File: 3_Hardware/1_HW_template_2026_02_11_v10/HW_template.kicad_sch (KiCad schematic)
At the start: 5 parts, among them P1 ${SIM.PARAMS}, P2 ${SIM.PARAMS}

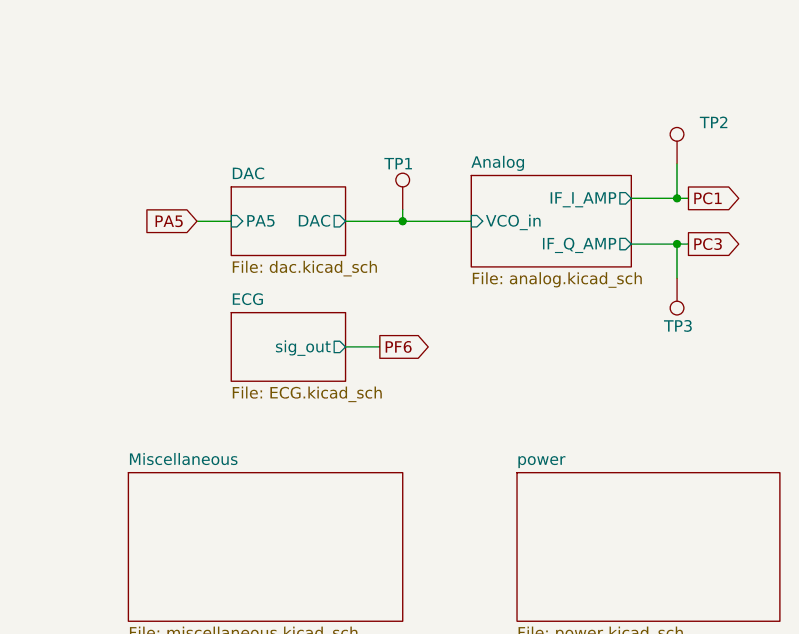
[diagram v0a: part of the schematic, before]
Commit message: pcb - minor naming improvements
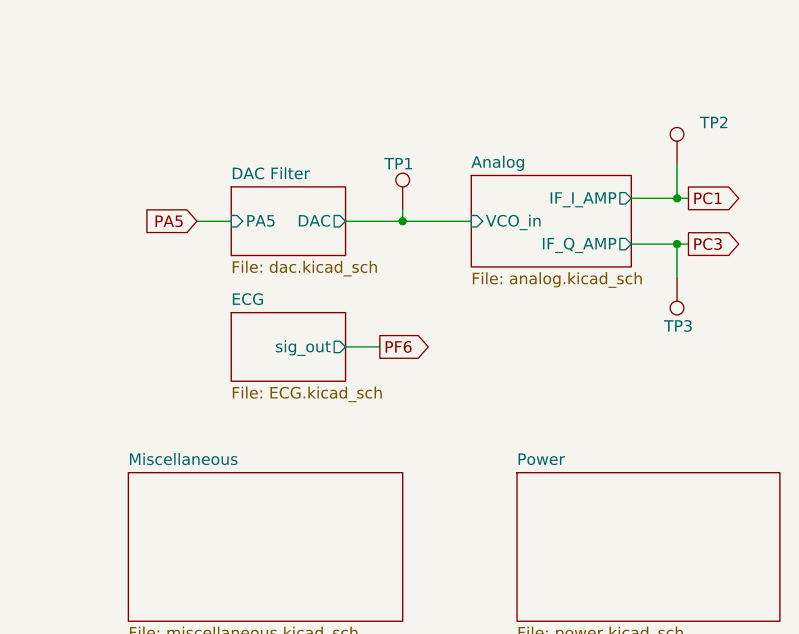
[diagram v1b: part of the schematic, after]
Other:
- sheet DAC renamed DAC Filter
- sheet power renamed Power
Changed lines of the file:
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@@
 			(color 0 0 0 0.0000)
 		)
-		(property "Sheetname" "power"
+		(property "Sheetname" "Power"
 			(at 187.96 99.6184 0)
 			(effects
@@
 			(color 0 0 0 0.0000)
 		)
-		(property "Sheetname" "DAC"
+		(property "Sheetname" "DAC Filter"
 			(at 156.21 67.8684 0)
 			(effects

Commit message: minor pcb improvements + bom
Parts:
- P1, P2: value ${SIM.PARAMS} -> Conn_01x32_Female
- TP1, TP2: value Channel1 -> ~
- TP3: value ${SIM.PARAMS} -> ~
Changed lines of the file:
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@@
 			)
 		)
-		(property "Value" "Channel1"
+		(property "Value" "~"
 			(at 177.8 69.0879 0)
 			(effects
@@
 			)
 		)
-		(property "Value" "${SIM.PARAMS}"
+		(property "Value" "Conn_01x32_Female"
 			(at 62.23 86.3601 0)
 			(effects
@@
 			)
 		)
-		(property "Value" "${SIM.PARAMS}"
+		(property "Value" "~"
 			(at 203.2 80.7721 0)
 			(effects
@@
 			)
 		)
-		(property "Value" "${SIM.PARAMS}"
+		(property "Value" "Conn_01x32_Female"
 			(at 24.13 86.3601 0)
 			(effects
@@
 			)
 		)
-		(property "Value" "Channel1"
+		(property "Value" "~"
 			(at 208.28 64.0079 0)
 			(effects

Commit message: pcb minor improvements
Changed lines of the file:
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@@
+	(wire
+		(pts
+			(xy 31.75 48.26) (xy 30.48 48.26)
+		)
+		(stroke
+			(width 0)
+			(type default)
+		)
+	)
 	(wire
 		(pts
@@
 	(symbol
 		(lib_id "power:GND")
-		(at 30.48 48.26 90)
+		(at 31.75 48.26 90)
 		(mirror x)
 		(unit 1)
@@
 		(fields_autoplaced yes)
 		(property "Reference" "#PWR01"
+			(at 38.1 48.26 0)
+			(effects
+				(font
+					(size 1.27 1.27)
+				)
+				(hide yes)
+			)
+		)
+		(property "Value" "GND"
 			(at 36.83 48.26 0)
 			(effects
@@
 					(size 1.27 1.27)
 				)
-				(hide yes)
-			)
-		)
-		(property "Value" "GND"
-			(at 35.56 48.26 0)
-			(effects
-				(font
-					(size 1.27 1.27)
-				)
 			)
 		)
 		(property "Footprint" ""
-			(at 30.48 48.26 0)
+			(at 31.75 48.26 0)
 			(effects
 				(font
@@
 		)
 		(property "Datasheet" ""
-			(at 30.48 48.26 0)
+			(at 31.75 48.26 0)
 			(effects
 				(font
@@
 		)
 		(property "Description" "Power symbol creates a global label with name \"GND\" , ground"
-			(at 30.48 48.26 0)
-			(effects
-				(font
+			(at 31.75 48.26 0)
+			(effects
+				(font
